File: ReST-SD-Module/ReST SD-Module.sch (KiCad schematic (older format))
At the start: 5 parts, among them CON1 SD_Card, P1 CONN_02X05

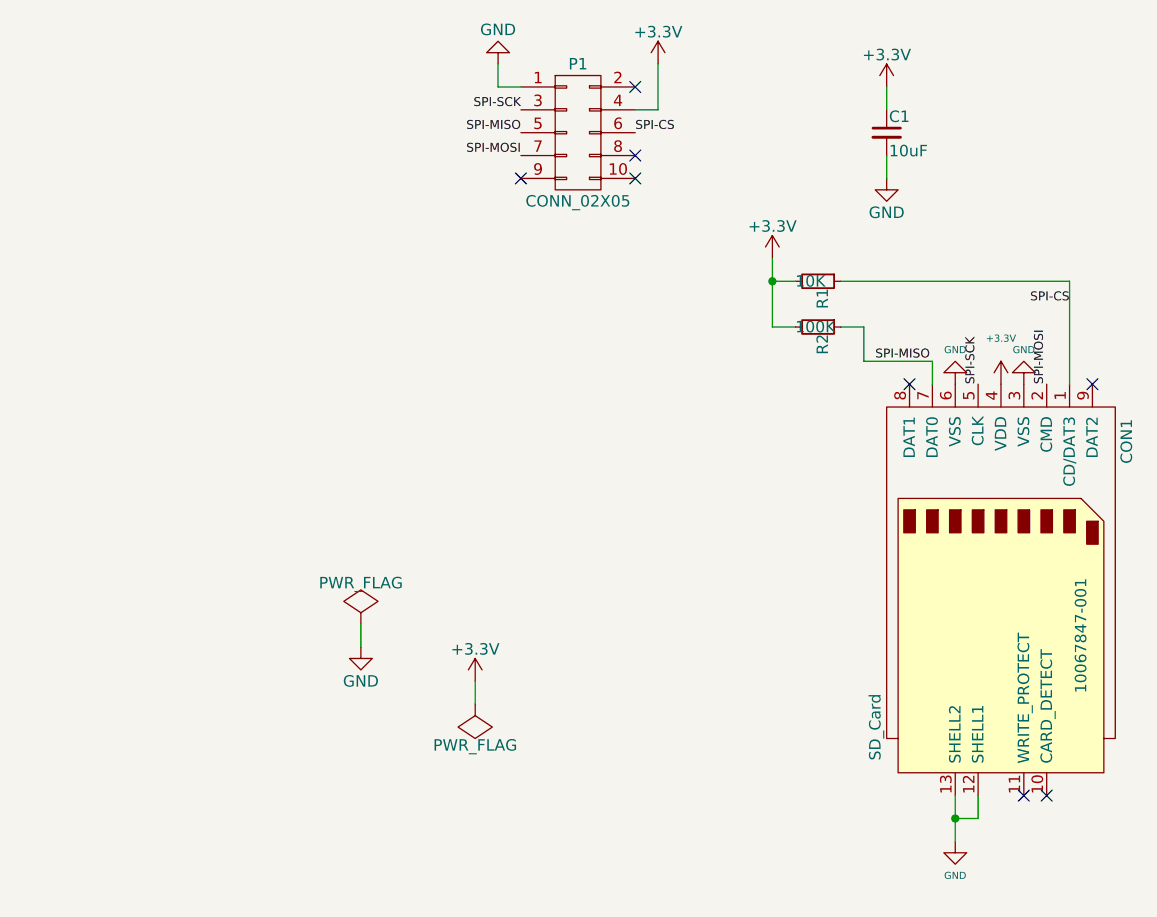
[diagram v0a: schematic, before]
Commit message: Removed unnecessary Libs and finished SD Card Module
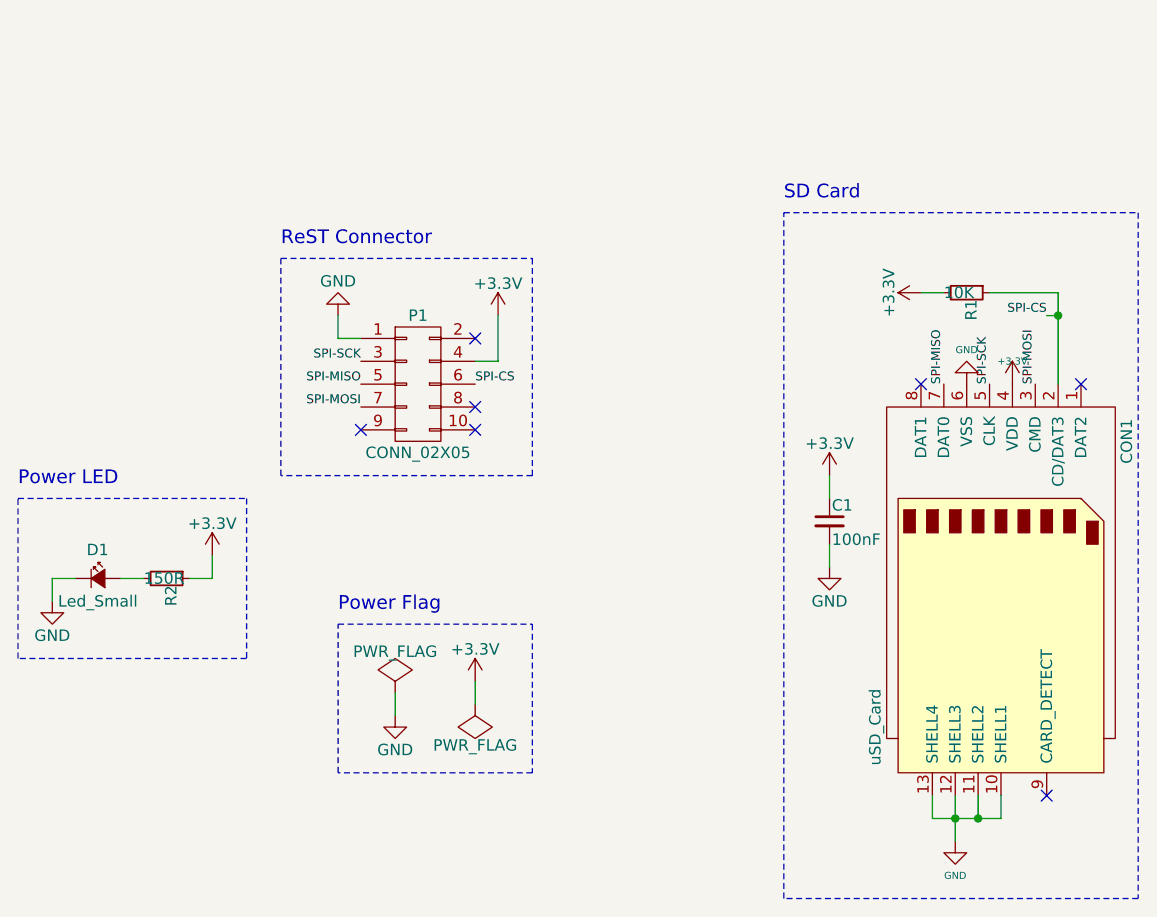
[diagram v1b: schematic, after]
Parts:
- removed CON1: SD_Card, 10067847-001, symbol SD_Card
- added CON1: uSD_Card, ReST-Library:uSD, symbol uSD_Card
- added D1: Led_Small, LEDs:LED_1206, symbol Led_Small
- C1: value 10uF -> 100nF; footprint (none) -> Capacitors_SMD:C_0805_HandSoldering
- P1: footprint (none) -> Pin_Headers:Pin_Header_Straight_2x05
- R1: footprint (none) -> Resistors_SMD:R_0805_HandSoldering
- R2: value 100K -> 150R; footprint (none) -> Resistors_SMD:R_0805_HandSoldering
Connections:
- net +3V3: now also R2.1, CON1.4 (VDD); no longer R2.2
- net GND: now also CON1.10 (SHELL1), CON1.11 (SHELL2), CON1.12 (SHELL3), CON1.13 (SHELL4), CON1.6 (VSS), D1.1 (K)
- net SPI-CS: now also CON1.2 (CD/DAT3)
- net SPI-MISO: now also CON1.7 (DAT0); no longer R2.1
- net SPI-MOSI: now also CON1.3 (CMD)
- net SPI-SCK: now also CON1.5 (CLK)
- new net: D1.2 (A), R2.2
- no-connect marks 8 -> 7
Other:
- note added: "Power Flag"
- note added: "Power LED"
- note added: "ReST Connector"
- note added: "SD Card"
- moved on the sheet: C1, P1, R1

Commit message: Added BOM for all Items + suggested Links
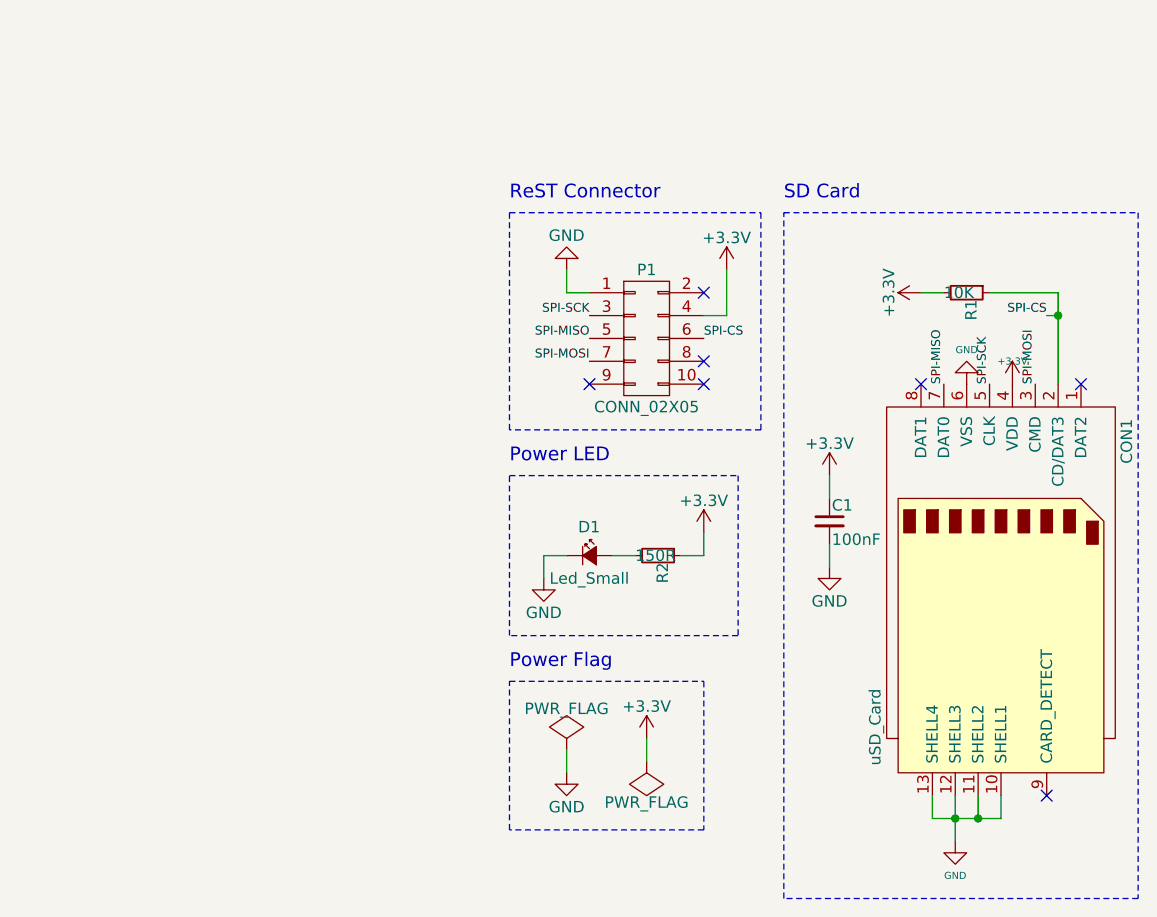
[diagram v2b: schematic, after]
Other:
- moved on the sheet: D1, P1, R2
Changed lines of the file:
@@
 encoding utf-8
 Sheet 1 1
-Title ""
-Date ""
-Rev ""
-Comp ""
+Title "ReST SD Module"
+Date "2016-03-06"
+Rev "Rev. A"
+Comp "Matthias Nowak"
 Comment1 ""
 Comment2 ""
@@
 L CONN_02X05 P1
 U 1 1 56D35E94
-P 3050 3050
-F 0 "P1" H 3050 3350 50  0000 C CNN
-F 1 "CONN_02X05" H 3050 2750 50  0000 C CNN
-F 2 "Pin_Headers:Pin_Header_Straight_2x05" H 3050 1850 50  0001 C CNN
-F 3 "" H 3050 1850 50  0000 C CNN
-	1    3050 3050
+P 4050 2850
+F 0 "P1" H 4050 3150 50  0000 C CNN
+F 1 "CONN_02X05" H 4050 2550 50  0000 C CNN
+F 2 "Pin_Headers:Pin_Header_Straight_2x05" H 4050 1650 50  0001 C CNN
+F 3 "" H 4050 1650 50  0000 C CNN
+	1    4050 2850
 	1    0    0    -1
 $EndComp
@@
 L GND #PWR01
 U 1 1 56D36072
-P 2950 4500
-F 0 "#PWR01" H 2950 4250 50  0001 C CNN
-F 1 "GND" H 2950 4350 50  0000 C CNN
-F 2 "" H 2950 4500 50  0000 C CNN
-F 3 "" H 2950 4500 50  0000 C CNN
-	1    2950 4500
+P 3700 4750
+F 0 "#PWR01" H 3700 4500 50  0001 C CNN
+F 1 "GND" H 3700 4600 50  0000 C CNN
+F 2 "" H 3700 4750 50  0000 C CNN
+F 3 "" H 3700 4750 50  0000 C CNN
+	1    3700 4750
 	1    0    0    -1
 $EndComp
@@
 L +3.3V #PWR02
 U 1 1 56D3608C
-P 3300 4350
-F 0 "#PWR02" H 3300 4200 50  0001 C CNN
-F 1 "+3.3V" H 3300 4490 50  0000 C CNN
-F 2 "" H 3300 4350 50  0000 C CNN
-F 3 "" H 3300 4350 50  0000 C CNN
-	1    3300 4350
+P 4050 4600
+F 0 "#PWR02" H 4050 4450 50  0001 C CNN
+F 1 "+3.3V" H 4050 4740 50  0000 C CNN
+F 2 "" H 4050 4600 50  0000 C CNN
+F 3 "" H 4050 4600 50  0000 C CNN
+	1    4050 4600
 	1    0    0    -1
 $EndComp
@@
 L PWR_FLAG #FLG03
 U 1 1 56D360A6
-P 3300 4450
-F 0 "#FLG03" H 3300 4545 50  0001 C CNN
-F 1 "PWR_FLAG" H 3300 4630 50  0000 C CNN
-F 2 "" H 3300 4450 50  0000 C CNN
-F 3 "" H 3300 4450 50  0000 C CNN
-	1    3300 4450
+P 4050 4700
+F 0 "#FLG03" H 4050 4795 50  0001 C CNN
+F 1 "PWR_FLAG" H 4050 4880 50  0000 C CNN
+F 2 "" H 4050 4700 50  0000 C CNN
+F 3 "" H 4050 4700 50  0000 C CNN
+	1    4050 4700
 	-1   0    0    1
 $EndComp
 Wire Wire Line
-	3300 4450 3300 4350
+	4050 4700 4050 4600
 $Comp
 L PWR_FLAG #FLG04
 U 1 1 56D360F9
-P 2950 4400
-F 0 "#FLG04" H 2950 4495 50  0001 C CNN
-F 1 "PWR_FLAG" H 2950 4580 50  0000 C CNN
-F 2 "" H 2950 4400 50  0000 C CNN
-F 3 "" H 2950 4400 50  0000 C CNN
-	1    2950 4400
-	1    0    0    -1
-$EndComp
-Wire Wire Line
-	2950 4400 2950 4500
+P 3700 4650
+F 0 "#FLG04" H 3700 4745 50  0001 C CNN
+F 1 "PWR_FLAG" H 3700 4830 50  0000 C CNN
+F 2 "" H 3700 4650 50  0000 C CNN
+F 3 "" H 3700 4650 50  0000 C CNN
+	1    3700 4650
+	1    0    0    -1
+$EndComp
+Wire Wire Line
+	3700 4650 3700 4750
 $Comp
 L GND #PWR05
 U 1 1 56D3613A
-P 2700 2750
-F 0 "#PWR05" H 2700 2500 50  0001 C CNN
-F 1 "GND" H 2700 2600 50  0000 C CNN
-F 2 "" H 2700 2750 50  0000 C CNN
-F 3 "" H 2700 2750 50  0000 C CNN
-	1    2700 2750
+P 3700 2550
+F 0 "#PWR05" H 3700 2300 50  0001 C CNN
+F 1 "GND" H 3700 2400 50  0000 C CNN
+F 2 "" H 3700 2550 50  0000 C CNN
+F 3 "" H 3700 2550 50  0000 C CNN
+	1    3700 2550
 	-1   0    0    1
 $EndComp
@@
 L +3.3V #PWR06
 U 1 1 56D36186
-P 3400 2750
-F 0 "#PWR06" H 3400 2600 50  0001 C CNN
-F 1 "+3.3V" H 3400 2890 50  0000 C CNN
-F 2 "" H 3400 2750 50  0000 C CNN
-F 3 "" H 3400 2750 50  0000 C CNN
-	1    3400 2750
-	1    0    0    -1
-$EndComp
-Wire Wire Line
-	3400 2750 3400 2950
-Wire Wire Line
-	2800 2850 2700 2850
-Wire Wire Line
-	2700 2850 2700 2750
-Text Label 2800 2950 2    39   ~ 0
+P 4400 2550
+F 0 "#PWR06" H 4400 2400 50  0001 C CNN
+F 1 "+3.3V" H 4400 2690 50  0000 C CNN
+F 2 "" H 4400 2550 50  0000 C CNN
+F 3 "" H 4400 2550 50  0000 C CNN
+	1    4400 2550
+	1    0    0    -1
+$EndComp
+Wire Wire Line
+	4400 2550 4400 2750
+Wire Wire Line
+	3800 2650 3700 2650
+Wire Wire Line
+	3700 2650 3700 2550
+Text Label 3800 2750 2    39   ~ 0
 SPI-SCK
-Text Label 2800 3050 2    39   ~ 0
+Text Label 3800 2850 2    39   ~ 0
 SPI-MISO
-Text Label 2800 3150 2    39   ~ 0
+Text Label 3800 2950 2    39   ~ 0
 SPI-MOSI
-Text Label 3300 3050 0    39   ~ 0
+Text Label 4300 2850 0    39   ~ 0
 SPI-CS
 Wire Wire Line
-	3400 2950 3300 2950
-NoConn ~ 3300 2850
-NoConn ~ 3300 3250
-NoConn ~ 3300 3150
+	4400 2750 4300 2750
+NoConn ~ 4300 2650
+NoConn ~ 4300 3050
+NoConn ~ 4300 2950
 $Comp
 L C_Small C1
@@
 NoConn ~ 5800 4850
 NoConn ~ 5250 3050
-NoConn ~ 2800 3250
+NoConn ~ 3800 3050
 Wire Notes Line
 	6200 2300 6200 5300
 Wire Notes Line
-	2450 2500 3550 2500
-Wire Notes Line
-	3550 2500 3550 3450
-Wire Notes Line
-	3550 3450 2450 3450
-Wire Notes Line
-	2450 3450 2450 2500
-Wire Notes Line
-	2700 4100 3550 4100
-Wire Notes Line
-	3550 4100 3550 4750
-Wire Notes Line
-	3550 4750 2700 4750
-Wire Notes Line
-	2700 4750 2700 4100
-Text Notes 2450 2450 0    60   ~ 0
+	3450 2300 4550 2300
+Wire Notes Line
+	4550 2300 4550 3250
+Wire Notes Line
+	4550 3250 3450 3250
+Wire Notes Line
+	3450 3250 3450 2300
+Wire Notes Line
+	3450 4350 4300 4350
+Wire Notes Line
+	4300 4350 4300 5000
+Wire Notes Line
+	4300 5000 3450 5000
+Wire Notes Line
+	3450 5000 3450 4350
+Text Notes 3450 2250 0    60   ~ 0
 ReST Connector
-Text Notes 2700 4050 0    60   ~ 0
+Text Notes 3450 4300 0    60   ~ 0
 Power Flag
 Text Notes 4650 2250 0    60   ~ 0
@@
 L Led_Small D1
 U 1 1 56D5E515
-P 1650 3900
-F 0 "D1" H 1600 4025 50  0000 L CNN
-F 1 "Led_Small" H 1475 3800 50  0000 L CNN
-F 2 "LEDs:LED_1206" V 1650 3900 50  0001 C CNN
-F 3 "" V 1650 3900 50  0000 C CNN
-	1    1650 3900
+P 3800 3800
+F 0 "D1" H 3750 3925 50  0000 L CNN
+F 1 "Led_Small" H 3625 3700 50  0000 L CNN
+F 2 "LEDs:LED_1206" V 3800 3800 50  0001 C CNN
+F 3 "" V 3800 3800 50  0000 C CNN
+	1    3800 3800
 	1    0    0    -1
 $EndComp
@@
 L R_Small R2
 U 1 1 56D5E568
-P 1950 3900
-F 0 "R2" H 1980 3920 50  0000 L CNN
-F 1 "150R" V 1950 3800 50  0000 L CNN
-F 2 "Resistors_SMD:R_0805_HandSoldering" H 1950 3900 50  0001 C CNN
-F 3 "" H 1950 3900 50  0000 C CNN
-	1    1950 3900
+P 4100 3800
+F 0 "R2" H 4130 3820 50  0000 L CNN
+F 1 "150R" V 4100 3700 50  0000 L CNN
+F 2 "Resistors_SMD:R_0805_HandSoldering" H 4100 3800 50  0001 C CNN
+F 3 "" H 4100 3800 50  0000 C CNN
+	1    4100 3800
 	0    1    1    0
 $EndComp
 Wire Wire Line
-	1750 3900 1850 3900
+	3900 3800 4000 3800
 $Comp
 L +3.3V #PWR013
 U 1 1 56D5E71A
-P 2150 3800
-F 0 "#PWR013" H 2150 3650 50  0001 C CNN
-F 1 "+3.3V" H 2150 3940 50  0000 C CNN
-F 2 "" H 2150 3800 50  0000 C CNN
-F 3 "" H 2150 3800 50  0000 C CNN
-	1    2150 3800
-	1    0    0    -1
-$EndComp
-Wire Wire Line
-	2050 3900 2150 3900
-Wire Wire Line
-	2150 3900 2150 3800
+P 4300 3700
+F 0 "#PWR013" H 4300 3550 50  0001 C CNN
+F 1 "+3.3V" H 4300 3840 50  0000 C CNN
+F 2 "" H 4300 3700 50  0000 C CNN
+F 3 "" H 4300 3700 50  0000 C CNN
+	1    4300 3700
+	1    0    0    -1
+$EndComp
+Wire Wire Line
+	4200 3800 4300 3800
+Wire Wire Line
+	4300 3800 4300 3700
 $Comp
 L GND #PWR014
 U 1 1 56D5E85D
-P 1450 4000
-F 0 "#PWR014" H 1450 3750 50  0001 C CNN
-F 1 "GND" H 1450 3850 50  0000 C CNN
-F 2 "" H 1450 4000 50  0000 C CNN
-F 3 "" H 1450 4000 50  0000 C CNN
-	1    1450 4000
-	1    0    0    -1
-$EndComp
-Wire Wire Line
-	1450 4000 1450 3900
-Wire Wire Line
-	1450 3900 1550 3900
-Wire Notes Line
-	1300 3550 2300 3550
-Wire Notes Line
-	2300 3550 2300 4250
-Wire Notes Line
-	2300 4250 1300 4250
-Wire Notes Line
-	1300 4250 1300 3550
-Text Notes 1300 3500 0    60   ~ 0
+P 3600 3900
+F 0 "#PWR014" H 3600 3650 50  0001 C CNN
+F 1 "GND" H 3600 3750 50  0000 C CNN
+F 2 "" H 3600 3900 50  0000 C CNN
+F 3 "" H 3600 3900 50  0000 C CNN
+	1    3600 3900
+	1    0    0    -1
+$EndComp
+Wire Wire Line
+	3600 3900 3600 3800
+Wire Wire Line
+	3600 3800 3700 3800
+Wire Notes Line
+	3450 3450 4450 3450
+Wire Notes Line
+	4450 3450 4450 4150
+Wire Notes Line
+	4450 4150 3450 4150
+Wire Notes Line
+	3450 4150 3450 3450
+Text Notes 3450 3400 0    60   ~ 0
 Power LED
 $Comp
